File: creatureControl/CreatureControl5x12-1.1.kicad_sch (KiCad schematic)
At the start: 49 parts, among them J1 USB_C_Receptacle_PowerOnly_6P, J10 Conn_01x02_Socket, J11 Conn_01x03_Socket, J12 Conn_01x05_Pin, J2 Barrel_Jack, J3 Screw_Terminal_01x02, J4 Conn_01x03_Socket, J5 Conn_01x03_Socket, J6 Conn_01x03_Socket, J7 Conn_01x03_Socket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

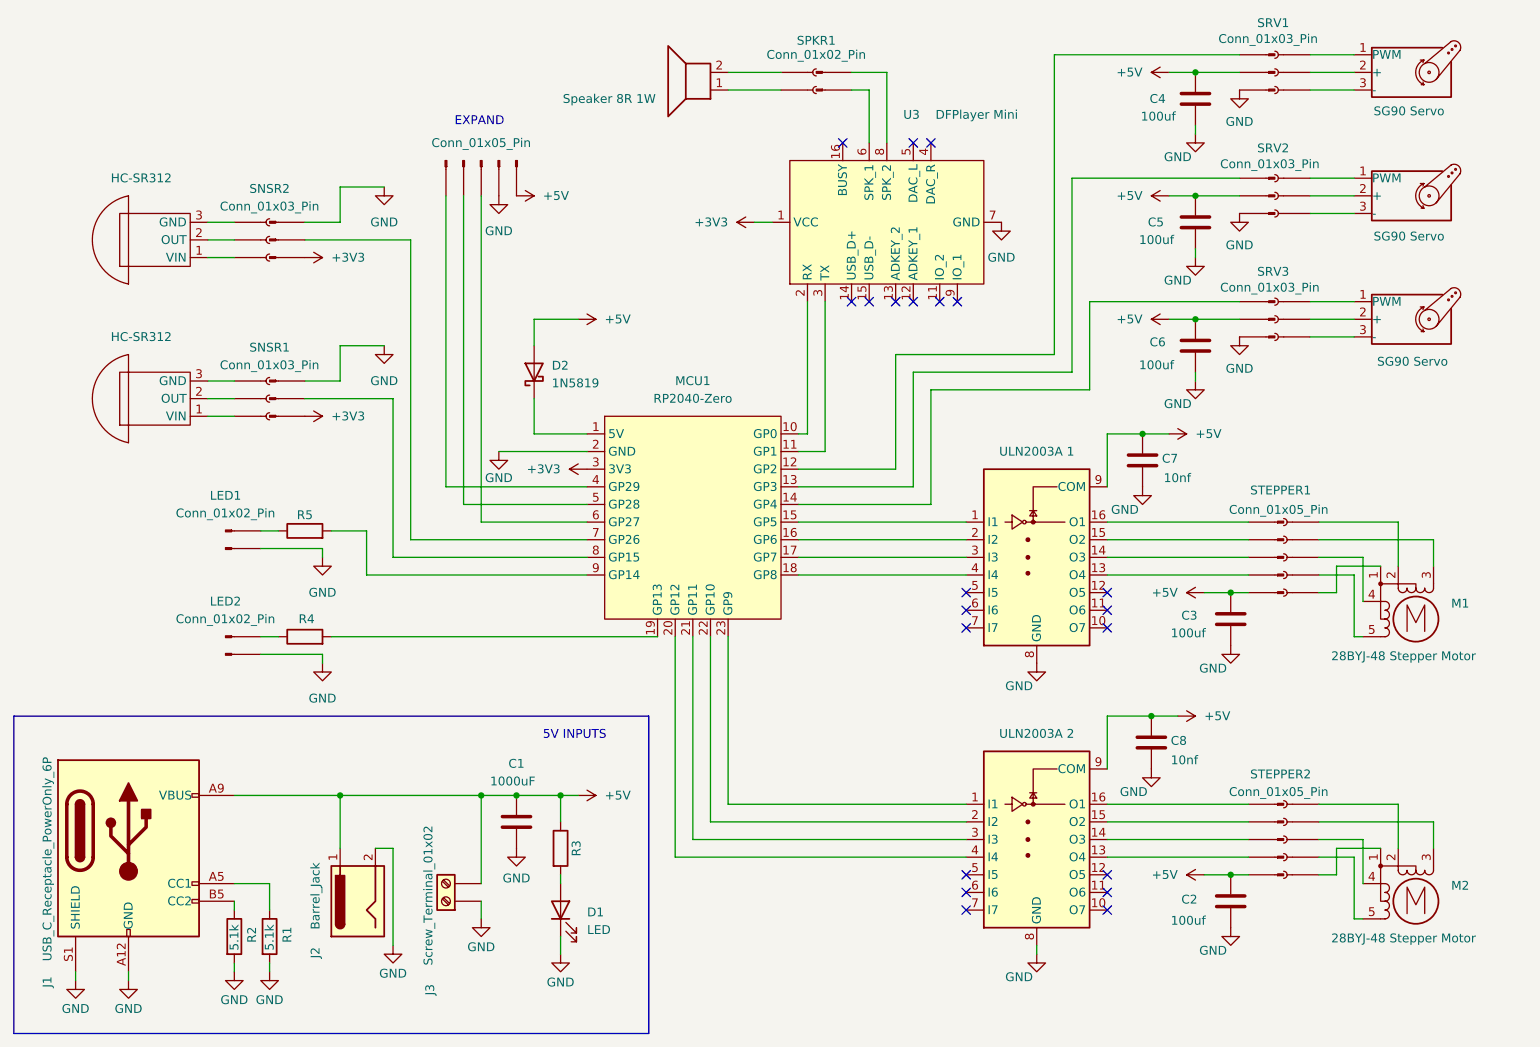
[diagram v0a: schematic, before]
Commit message: Update CC5x12 to v1.1
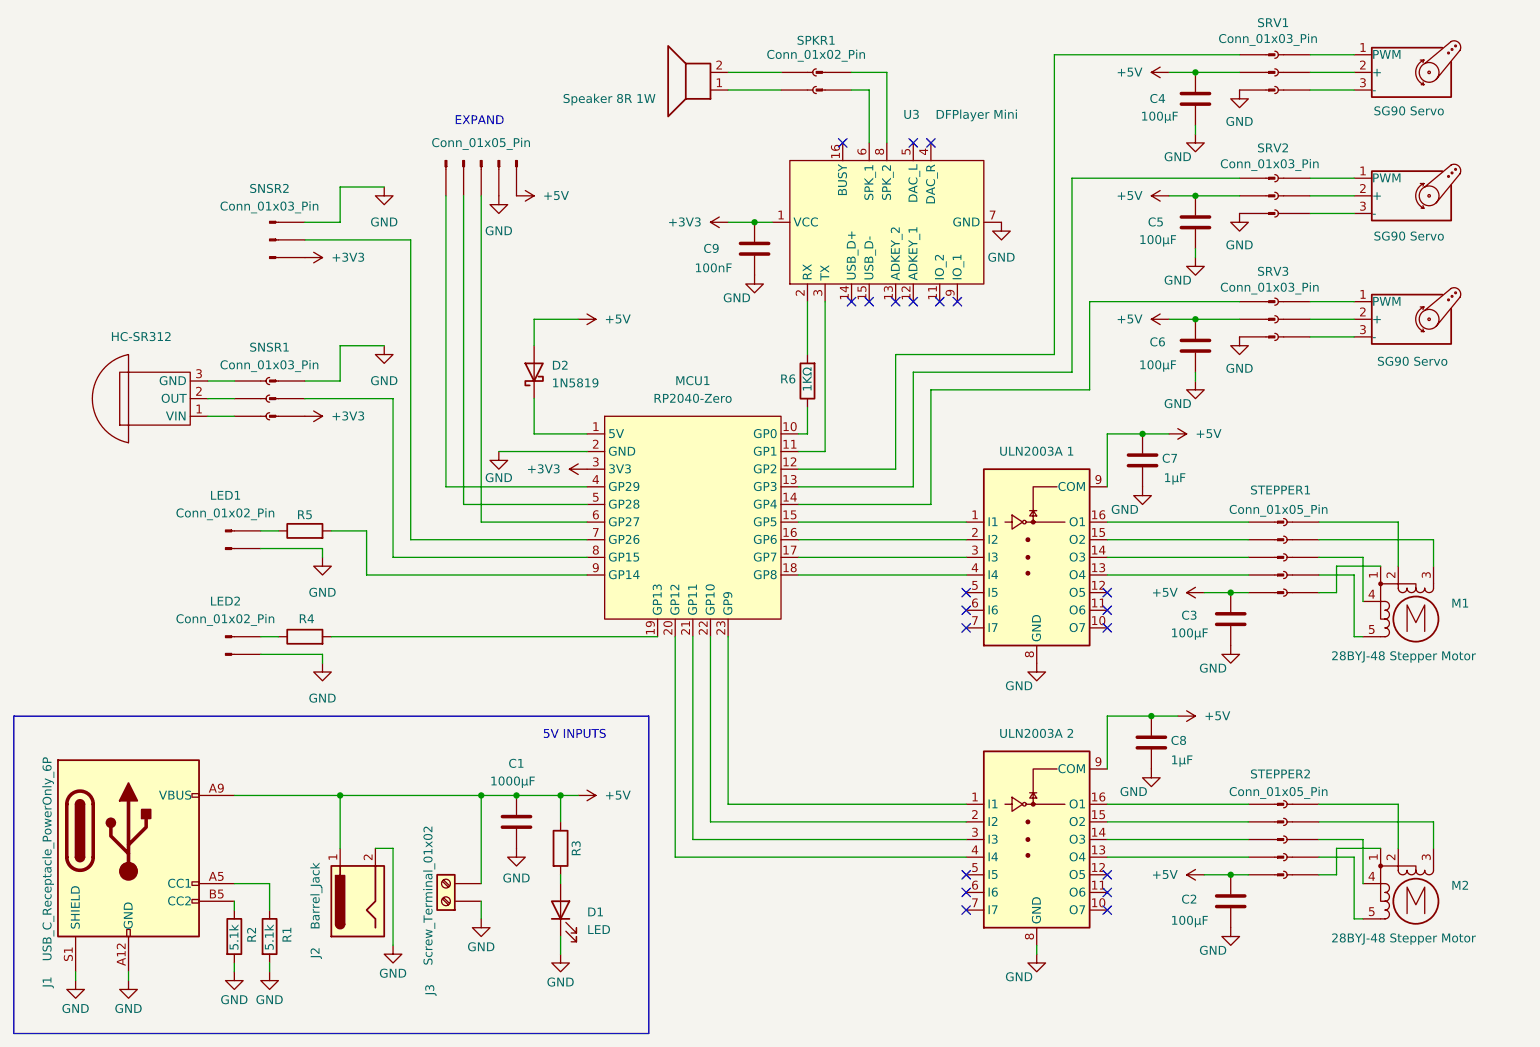
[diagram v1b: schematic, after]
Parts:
- removed J11: Conn_01x03_Socket, symbol Connector:Conn_01x03_Socket
- removed SNS2: HC-SR312, symbol Ken_Library:HC-SR312
- added C9: 100nF, symbol Device:C
- added R6: 1KΩ, symbol Device:R
- C1: value 1000uF -> 1000µF
- C2, C3, C4, C5, C6: value 100uf -> 100µF
- C7, C8: value 10nf -> 1µF
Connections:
- net +3V3: now also C9.2
- net GND: now also C9.1
- net at MCU1.10 (GP0): now also R6.1; no longer U3.2 (RX)
- new net: R6.2, U3.2 (RX)
